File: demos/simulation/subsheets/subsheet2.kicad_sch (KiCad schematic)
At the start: 5 parts

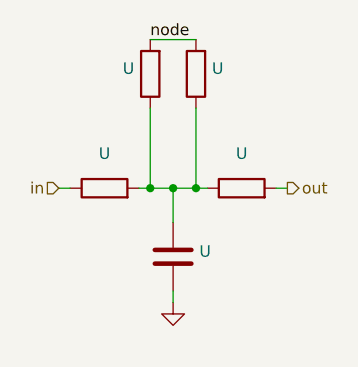
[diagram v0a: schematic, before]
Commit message: feat: update kicad to 9.0.0+dfsg-1
Signed-off-by: lhdjply <lhdjply@126.com>
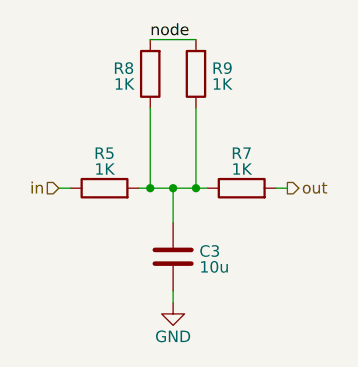
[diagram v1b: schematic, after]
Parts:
- C3: renamed from U; value (none) -> 10u
- R5, R7, R8, R9: renamed from U; value (none) -> 1K
